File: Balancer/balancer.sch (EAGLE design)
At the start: 285 parts, among them Q1 BSS123W, Q10A SIR882DP-T1-GE3, Q10B SIS468DN-T1-GE3, Q11A SIR882DP-T1-GE3, Q11B SIS468DN-T1-GE3, Q12A SIR882DP-T1-GE3, Q12B SIS468DN-T1-GE3, Q2 BSS123W, Q3A SIR882DP-T1-GE3, Q3B SIS468DN-T1-GE3, Q4 MMBT3906LT1G, Q4A SIR882DP-T1-GE3, Q4B SIS468DN-T1-GE3, Q5 FDN5618P, Q5A SIR882DP-T1-GE3, Q5B SIS468DN-T1-GE3, Q6 CMPT3904E_TR_PBFREE, Q6A SIR882DP-T1-GE3, Q6B SIS468DN-T1-GE3, Q9A SIR882DP-T1-GE3, Q9B SIS468DN-T1-GE3, T10 750312504, T11 750312504, T12 750312504, T3 750312504, T4 750312504, T5 750312504, T6 750312504, T9 750312504, U1 LTC3300ILXE-1PBF, U2 LTC3300ILXE-1PBF

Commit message: done final check, generated Gerber file
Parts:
- renumbered CN1 to BATT, CN2 to VOLT_TAPS, JP1 to COMM, TP1 to WDTA, TP2 to WDTC
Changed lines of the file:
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@@
 <part name="E8" library="Turret" deviceset="2501-2-00-80-00-00-07-0" device=""/>
 <part name="E15" library="Turret" deviceset="2501-2-00-80-00-00-07-0" device=""/>
-<part name="CN1" library="jst-vh" deviceset="B9P-VH" device=""/>
+<part name="BATT" library="jst-vh" deviceset="B9P-VH" device=""/>
 <part name="F12" library="01530008Z" deviceset="01530008Z" device=""/>
 <part name="F11" library="01530008Z" deviceset="01530008Z" device=""/>
@@
 <part name="C6" library="rcl" library_urn="urn:adsk.eagle:library:334" deviceset="C-US" device="C1210" package3d_urn="urn:adsk.eagle:package:23619/2" value="4.7uF"/>
 <part name="R7" library="Ilya_Teach" deviceset="RES" device="" value="1M"/>
-<part name="TP1" library="Turret" deviceset="2501-2-00-80-00-00-07-0" device=""/>
-<part name="TP2" library="Turret" deviceset="2501-2-00-80-00-00-07-0" device=""/>
+<part name="WDTA" library="Turret" deviceset="2501-2-00-80-00-00-07-0" device=""/>
+<part name="WDTC" library="Turret" deviceset="2501-2-00-80-00-00-07-0" device=""/>
 <part name="Q2" library="BSS123W" deviceset="BSS123W" device=""/>
 <part name="R8" library="Ilya_Teach" deviceset="RES" device="" value="1.27M"/>
@@
 <part name="R55" library="Ilya_Teach" deviceset="RES" device="" value="20"/>
 <part name="D11" library="adafruit" deviceset="DIODE" device="SOD-323F" value="PDZ5.6B"/>
-<part name="CN2" library="jst-vh" deviceset="B9P-VH" device=""/>
-<part name="JP1" library="Connector" library_urn="urn:adsk.eagle:library:16378166" deviceset="PINHD-1X4" device="" package3d_urn="urn:adsk.eagle:package:51802636/2"/>
+<part name="VOLT_TAPS" library="jst-vh" deviceset="B9P-VH" device=""/>
+<part name="COMM" library="Connector" library_urn="urn:adsk.eagle:library:16378166" deviceset="PINHD-1X4" device="" package3d_urn="urn:adsk.eagle:package:51802636/2"/>
 <part name="R11" library="rcl" library_urn="urn:adsk.eagle:library:334" deviceset="R-US_" device="R2512" package3d_urn="urn:adsk.eagle:package:23545/2" value="0"/>
 <part name="R12" library="rcl" library_urn="urn:adsk.eagle:library:334" deviceset="R-US_" device="R2512" package3d_urn="urn:adsk.eagle:package:23545/2" value="0"/>
@@
 <attribute name="NAME" x="-116.33153125" y="160.020790625" size="1.77828125" layer="95" rot="R270"/>
 </instance>
-<instance part="CN1" gate="G$1" x="-248.92" y="83.82" smashed="yes">
+<instance part="BATT" gate="G$1" x="-248.92" y="83.82" smashed="yes">
 <attribute name="NAME" x="-252.73" y="97.79" size="1.778" layer="95"/>
 <attribute name="VALUE" x="-252.73" y="68.58" size="1.778" layer="96"/>
@@
 <attribute name="VALUE" x="76.962" y="8.89" size="1.778" layer="96" rot="R90"/>
 </instance>
-<instance part="TP1" gate="G$1" x="91.44" y="106.68" smashed="yes">
+<instance part="WDTA" gate="G$1" x="91.44" y="106.68" smashed="yes">
 <attribute name="NAME" x="86.359209375" y="109.72846875" size="1.77828125" layer="95"/>
 </instance>
-<instance part="TP2" gate="G$1" x="40.64" y="17.78" smashed="yes" rot="R180">
+<instance part="WDTC" gate="G$1" x="40.64" y="17.78" smashed="yes" rot="R180">
 <attribute name="NAME" x="45.720790625" y="14.73153125" size="1.77828125" layer="95" rot="R180"/>
 </instance>
@@
 <attribute name="NAME" x="101.6" y="50.8" size="1.27" layer="95" rot="R180"/>
 </instance>
-<instance part="CN2" gate="G$1" x="-172.72" y="25.4" smashed="yes" rot="MR0">
+<instance part="VOLT_TAPS" gate="G$1" x="-172.72" y="25.4" smashed="yes" rot="MR0">
 <attribute name="NAME" x="-168.91" y="39.37" size="1.778" layer="95" rot="MR0"/>
 <attribute name="VALUE" x="-168.91" y="10.16" size="1.778" layer="96" rot="MR0"/>
 </instance>
-<instance part="JP1" gate="A" x="-30.48" y="48.26" smashed="yes" rot="R180">
+<instance part="COMM" gate="A" x="-30.48" y="48.26" smashed="yes" rot="R180">
 <attribute name="NAME" x="-30.48" y="38.1" size="1.778" layer="95" rot="R180" align="top-center"/>
 <attribute name="VALUE" x="-30.48" y="55.88" size="1.778" layer="96" rot="R180" align="bottom-center"/>
@@
 </segment>
 <segment>
-<pinref part="CN2" gate="G$1" pin="5"/>
+<pinref part="VOLT_TAPS" gate="G$1" pin="5"/>
 <wire x1="-167.64" y1="25.4" x2="-172.72" y2="25.4" width="0.1524" layer="91"/>
 <label x="-167.64" y="25.4" size="1.778" layer="95"/>
@@
 </segment>
 <segment>
-<pinref part="CN2" gate="G$1" pin="3"/>
+<pinref part="VOLT_TAPS" gate="G$1" pin="3"/>
 <wire x1="-167.64" y1="30.48" x2="-172.72" y2="30.48" width="0.1524" layer="91"/>
 <label x="-167.64" y="30.48" size="1.778" layer="95"/>
@@
 </segment>
 <segment>
-<pinref part="JP1" gate="A" pin="4"/>
+<pinref part="COMM" gate="A" pin="4"/>
 <label x="-22.86" y="50.8" size="1.778" layer="95"/>
 <pinref part="U1" gate="A" pin="CTRL"/>
@@
 </segment>
 <segment>
-<pinref part="CN2" gate="G$1" pin="1"/>
+<pinref part="VOLT_TAPS" gate="G$1" pin="1"/>
 <wire x1="-167.64" y1="35.56" x2="-172.72" y2="35.56" width="0.1524" layer="91"/>
 <label x="-167.64" y="35.56" size="1.778" layer="95"/>
@@
 </segment>
 <segment>
-<pinref part="CN2" gate="G$1" pin="4"/>
+<pinref part="VOLT_TAPS" gate="G$1" pin="4"/>
 <wire x1="-167.64" y1="27.94" x2="-172.72" y2="27.94" width="0.1524" layer="91"/>
 <label x="-167.64" y="27.94" size="1.778" layer="95"/>
@@
 </segment>
 <segment>
-<pinref part="CN2" gate="G$1" pin="2"/>
+<pinref part="VOLT_TAPS" gate="G$1" pin="2"/>
 <wire x1="-167.64" y1="33.02" x2="-172.72" y2="33.02" width="0.1524" layer="91"/>
 <label x="-167.64" y="33.02" size="1.778" layer="95"/>
@@
 <junction x="-5.08" y="40.64"/>
 <junction x="-5.08" y="43.18"/>
-<pinref part="JP1" gate="A" pin="1"/>
+<pinref part="COMM" gate="A" pin="1"/>
 <wire x1="-5.08" y1="43.18" x2="-25.4" y2="43.18" width="0.1524" layer="91"/>
 </segment>
@@
 <pinref part="U1" gate="A" pin="CSBI"/>
 <label x="-7.62" y="48.26" size="1.778" layer="95"/>
-<pinref part="JP1" gate="A" pin="3"/>
+<pinref part="COMM" gate="A" pin="3"/>
 <wire x1="-5.08" y1="48.26" x2="-25.4" y2="48.26" width="0.1524" layer="91"/>
 </segment>
@@
 <pinref part="U1" gate="A" pin="SCKI"/>
 <label x="-7.62" y="45.72" size="1.778" layer="95"/>
-<pinref part="JP1" gate="A" pin="2"/>
+<pinref part="COMM" gate="A" pin="2"/>
 <wire x1="-5.08" y1="45.72" x2="-25.4" y2="45.72" width="0.1524" layer="91"/>
 </segment>
@@
 <pinref part="Q1" gate="G$1" pin="S"/>
 <wire x1="81.28" y1="111.76" x2="81.28" y2="106.68" width="0.1524" layer="91"/>
-<pinref part="TP1" gate="G$1" pin="1"/>
+<pinref part="WDTA" gate="G$1" pin="1"/>
 <junction x="81.28" y="106.68"/>
 </segment>
@@
 </segment>
 <segment>
-<pinref part="CN2" gate="G$1" pin="6"/>
+<pinref part="VOLT_TAPS" gate="G$1" pin="6"/>
 <wire x1="-167.64" y1="22.86" x2="-172.72" y2="22.86" width="0.1524" layer="91"/>
 <label x="-167.64" y="22.86" size="1.778" layer="95"/>
@@
 </segment>
 <segment>
-<pinref part="CN2" gate="G$1" pin="7"/>
+<pinref part="VOLT_TAPS" gate="G$1" pin="7"/>
 <wire x1="-167.64" y1="20.32" x2="-172.72" y2="20.32" width="0.1524" layer="91"/>
 <label x="-167.64" y="20.32" size="1.778" layer="95"/>
@@
 </segment>
 <segment>
-<pinref part="CN2" gate="G$1" pin="8"/>
+<pinref part="VOLT_TAPS" gate="G$1" pin="8"/>
 <wire x1="-167.64" y1="17.78" x2="-172.72" y2="17.78" width="0.1524" layer="91"/>
 <label x="-167.64" y="17.78" size="1.778" layer="95"/>
@@
 </segment>
 <segment>
-<pinref part="CN2" gate="G$1" pin="9"/>
+<pinref part="VOLT_TAPS" gate="G$1" pin="9"/>
 <wire x1="-167.64" y1="15.24" x2="-172.72" y2="15.24" width="0.1524" layer="91"/>
 <label x="-167.64" y="15.24" size="1.778" layer="95"/>
@@
 <net name="BAT+" class="0">
 <segment>
-<pinref part="CN1" gate="G$1" pin="1"/>
+<pinref part="BATT" gate="G$1" pin="1"/>
 <pinref part="F12" gate="G$1" pin="2"/>
 <wire x1="-238.76" y1="93.98" x2="-248.92" y2="93.98" width="0.1524" layer="91"/>
@@
 <net name="N$14" class="0">
 <segment>
-<pinref part="CN1" gate="G$1" pin="2"/>
+<pinref part="BATT" gate="G$1" pin="2"/>
 <pinref part="F11" gate="G$1" pin="1"/>
 <wire x1="-254" y1="91.44" x2="-248.92" y2="91.44" width="0.1524" layer="91"/>
@@
 <net name="N$18" class="0">
 <segment>
-<pinref part="CN1" gate="G$1" pin="3"/>
+<pinref part="BATT" gate="G$1" pin="3"/>
 <pinref part="F10" gate="G$1" pin="2"/>
 <wire x1="-246.38" y1="88.9" x2="-248.92" y2="88.9" width="0.1524" layer="91"/>
@@
 <net name="N$22" class="0">
 <segment>
-<pinref part="CN1" gate="G$1" pin="4"/>
+<pinref part="BATT" gate="G$1" pin="4"/>
 <pinref part="F9" gate="G$1" pin="1"/>
 </segment>
@@
 <net name="N$23" class="0">
 <segment>
-<pinref part="CN1" gate="G$1" pin="5"/>
+<pinref part="BATT" gate="G$1" pin="5"/>
 <pinref part="F6" gate="G$1" pin="2"/>
 <wire x1="-238.76" y1="83.82" x2="-248.92" y2="83.82" width="0.1524" layer="91"/>
@@
 <net name="N$25" class="0">
 <segment>
-<pinref part="CN1" gate="G$1" pin="6"/>
+<pinref part="BATT" gate="G$1" pin="6"/>
 <pinref part="F5" gate="G$1" pin="1"/>
 <wire x1="-254" y1="81.28" x2="-248.92" y2="81.28" width="0.1524" layer="91"/>
@@
 <net name="N$26" class="0">
 <segment>
-<pinref part="CN1" gate="G$1" pin="7"/>
+<pinref part="BATT" gate="G$1" pin="7"/>
 <pinref part="F4" gate="G$1" pin="2"/>
 <wire x1="-246.38" y1="78.74" x2="-248.92" y2="78.74" width="0.1524" layer="91"/>
@@
 <net name="N$28" class="0">
 <segment>
-<pinref part="CN1" gate="G$1" pin="8"/>
+<pinref part="BATT" gate="G$1" pin="8"/>
 <pinref part="F3" gate="G$1" pin="1"/>
 </segment>
@@
 <net name="N$30" class="0">
 <segment>
-<pinref part="CN1" gate="G$1" pin="9"/>
+<pinref part="BATT" gate="G$1" pin="9"/>
 <pinref part="F15" gate="G$1" pin="2"/>
 <wire x1="-238.76" y1="73.66" x2="-248.92" y2="73.66" width="0.1524" layer="91"/>
@@
 <pinref part="R7" gate="G$1" pin="2"/>
 <wire x1="73.66" y1="17.78" x2="50.8" y2="17.78" width="0.1524" layer="91"/>
-<pinref part="TP2" gate="G$1" pin="1"/>
+<pinref part="WDTC" gate="G$1" pin="1"/>
 <label x="73.66" y="17.78" size="1.778" layer="95"/>
 <pinref part="Q2" gate="G$1" pin="S"/>

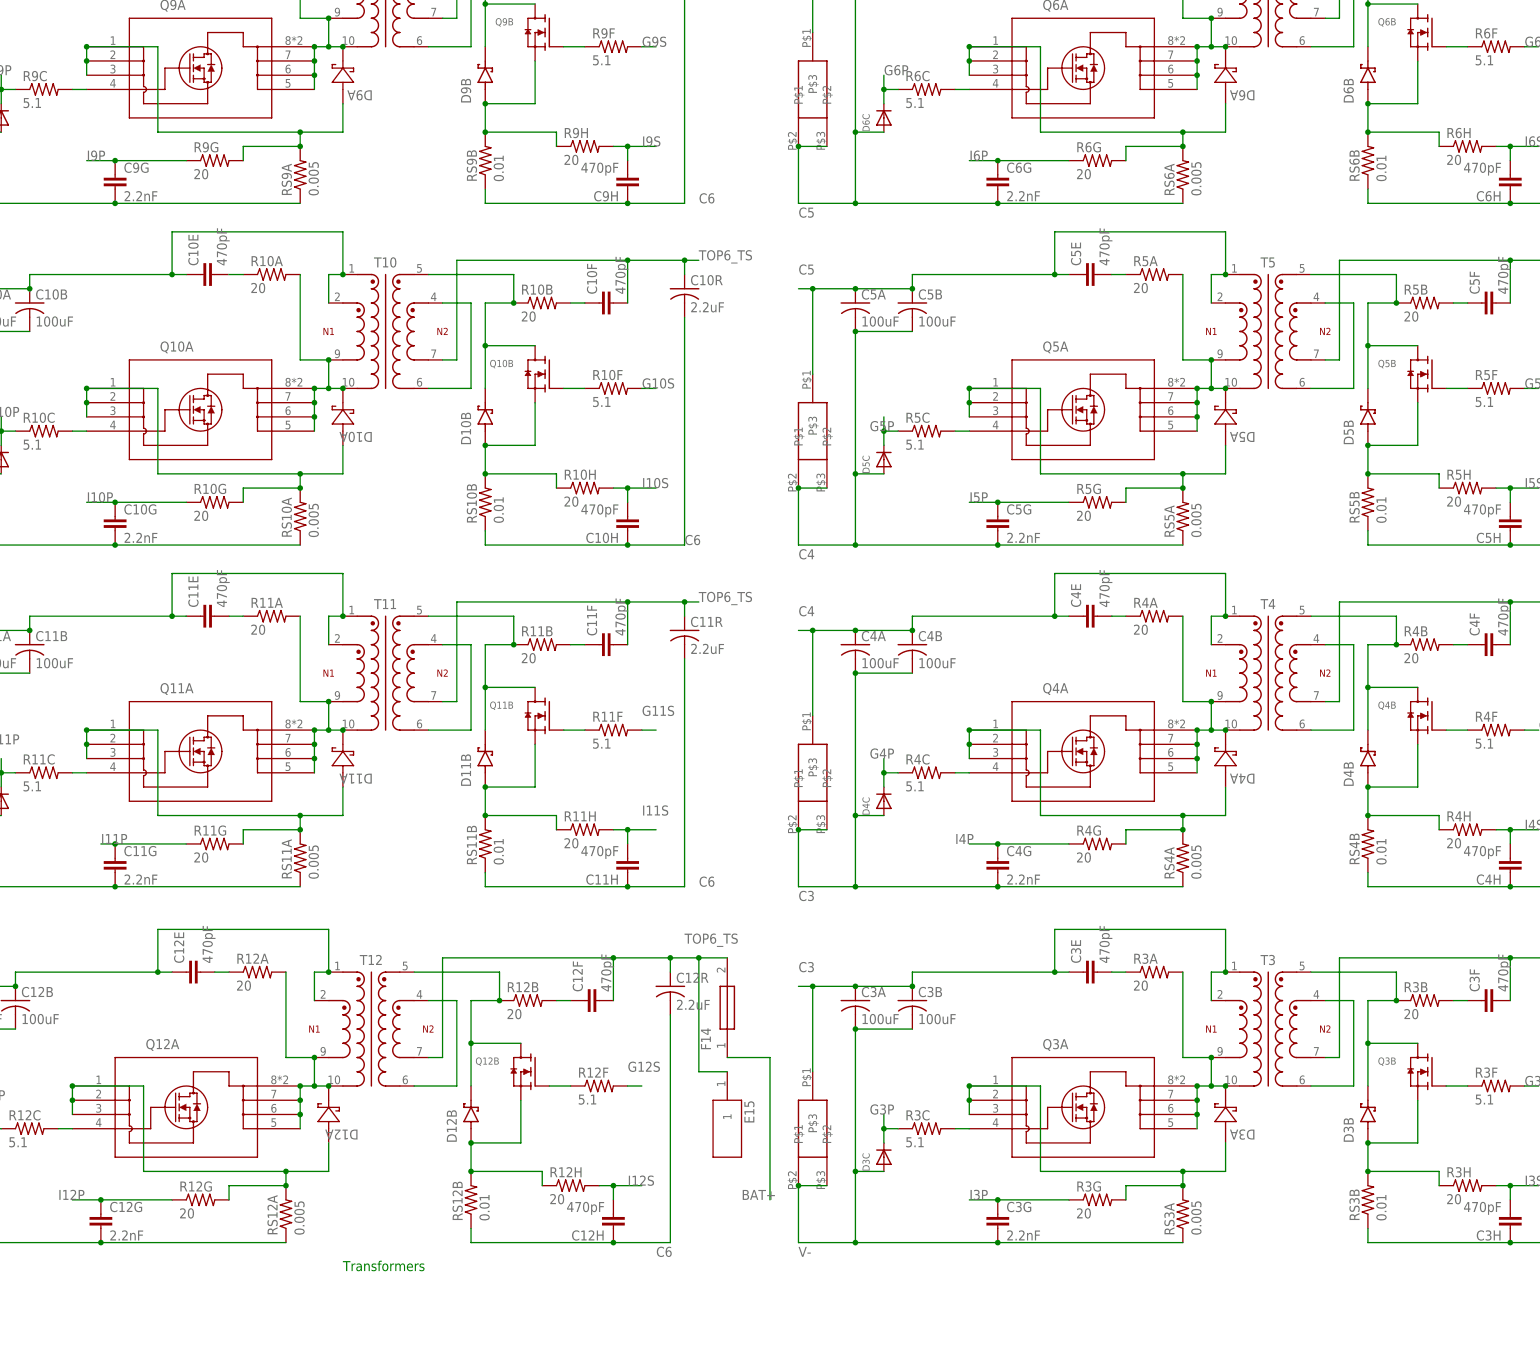
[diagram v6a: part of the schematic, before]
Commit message: replaced RSnA and RSnB to correct parts
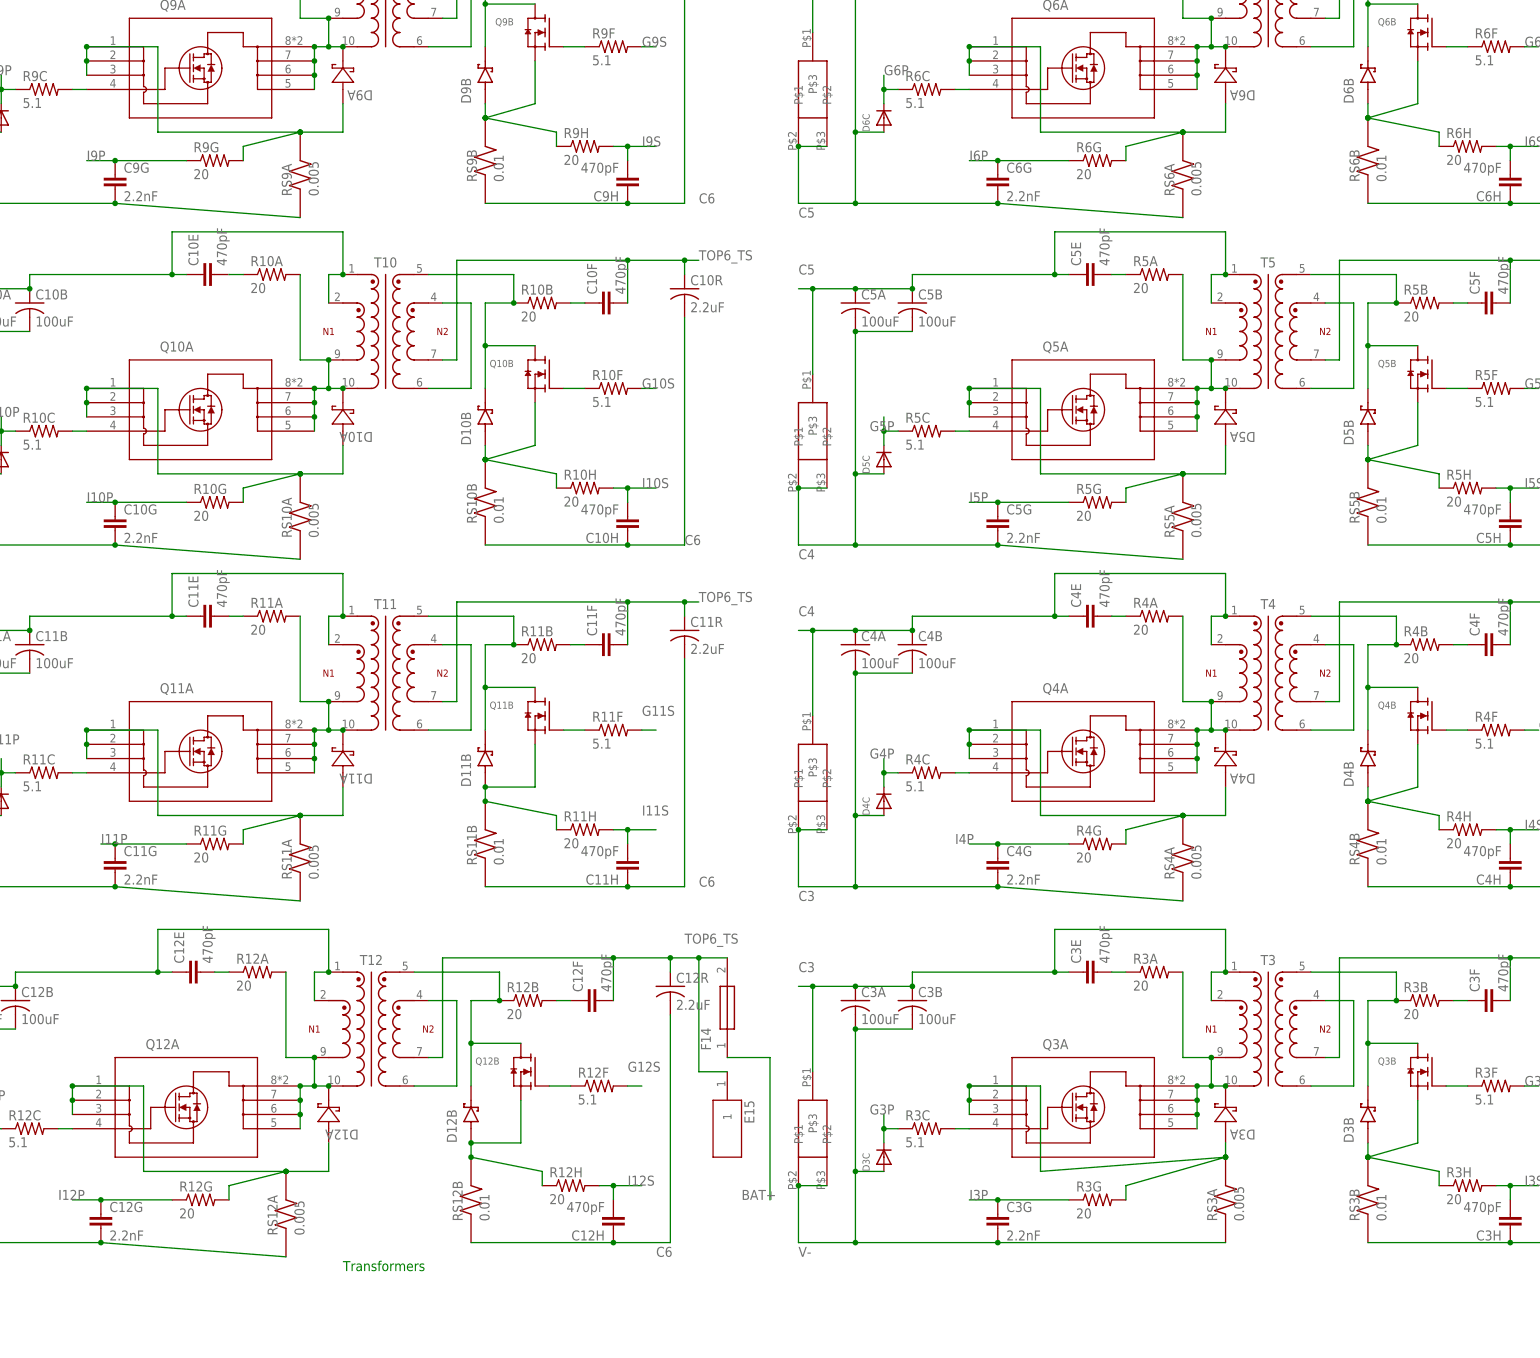
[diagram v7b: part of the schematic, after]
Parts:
- RS10A, RS10B, RS11A, RS11B, RS12A, RS12B, RS3A, RS3B, RS4A, RS4B, RS5A, RS5B, RS6A, RS6B, RS9A, RS9B: device rcl:R-US_R1206 -> PRL1632-R010-F-T1:PRL1632-R010-F-T1

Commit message: random updates
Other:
- moved on the sheet: C1, C10, C10K, C11, C11K, C12, C12K, C13, C15, C16, C17, C18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
